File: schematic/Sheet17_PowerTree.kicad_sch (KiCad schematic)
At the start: 11 parts

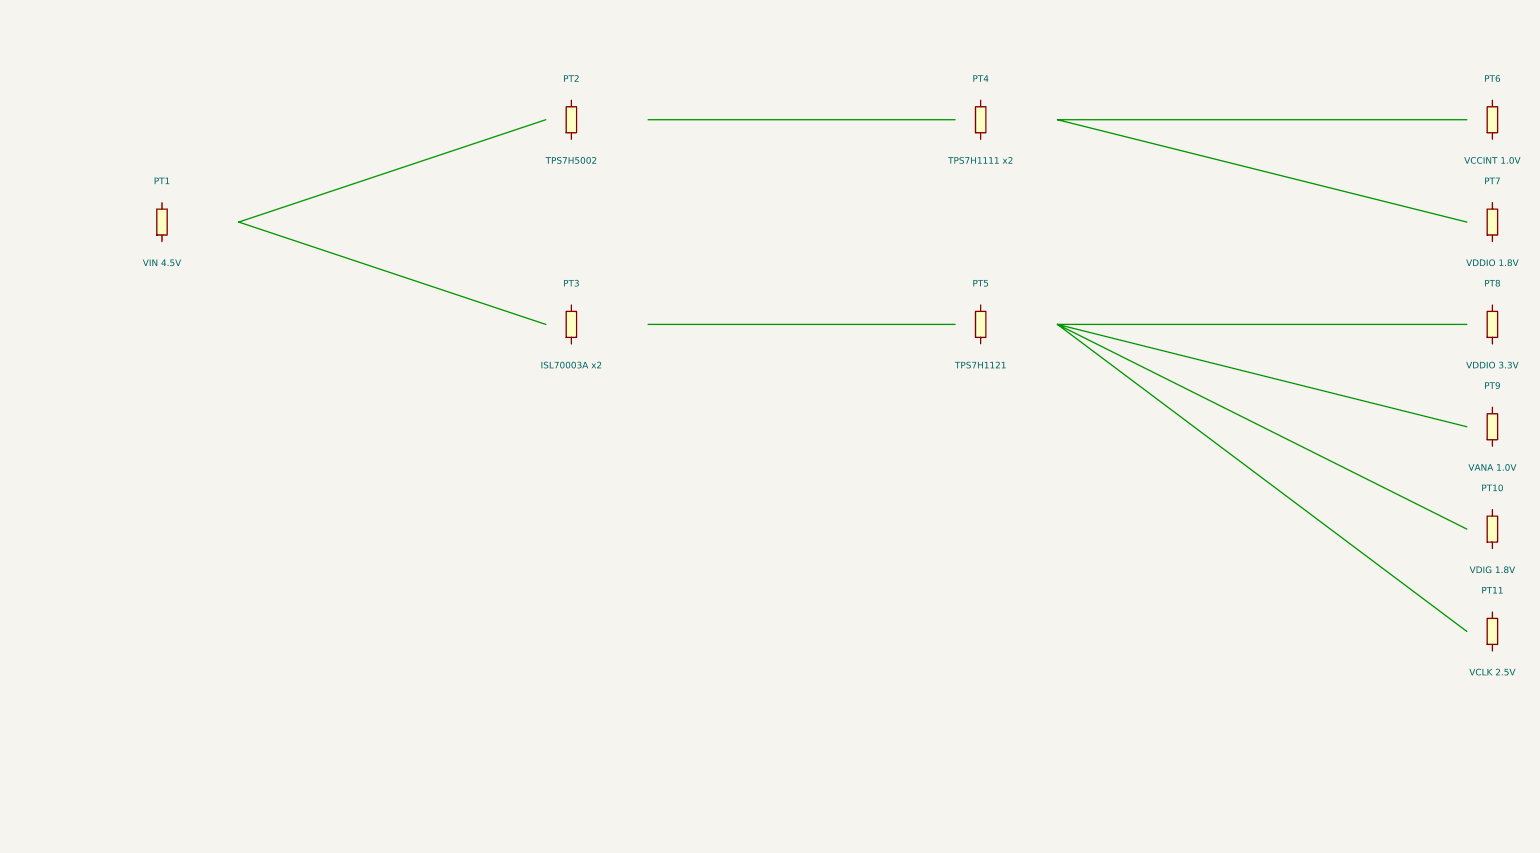
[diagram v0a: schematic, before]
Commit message: feat: real IC schematics with proper pin connections
- ADC12DJ5200-SP: 20 left pins (power, SPI, analog) + 21 right pins (JESD204C)
- XQRVC1902-SP: 19 left pins (power) + 30 right pins (JTAG, SPW, JESD, config)
- TPS7H5002-SP: 9 left + 7 right pins (buck converter 1.0V core)
- ISL70003ASEH: 7 left + 5 right (buck 1.8V/3.3V)
- LMX2615-SP: 8+8 pins (PLL synthesizer)
- LMK04832-SP: 12+12 pins (clock distributor)
- TPS7H1111-SP / TPS7H1121-SP: 3+3 pins (LDOs)
- TPS7H3014-SP: 4+4 pins (sequencer)
- INA214-SP: 3+2 pins (current sense)
- CVHD-950: 3+2 pins (VCXO)

Sheets:
- 02: SMA→50Ω match→anti-alias→ADC analog input
- 03: ADC decoupling, JESD outputs, SPI control
- 04: FPGA 14x decoupling caps, JTAG, SPW, JESD
- 05: Crystek→LMX2615→LMK04832→ADC+FPGA clock tree
- 06-09: Power input, TPS7H5002 buck 1.0V, ISL70003A buck 1.8V/3.3V
- 10-12: LDO 1.0V analog, 1.8V digital, 2.5V clock
- 13: 2x TPS7H3014 power sequencer
- 14: JTAG/SPW/UART connectors
- 15-17: Test points, decoupling, power tree diagram

All 17 sheets export via kicad-cli, merged PDF: 1.1MB
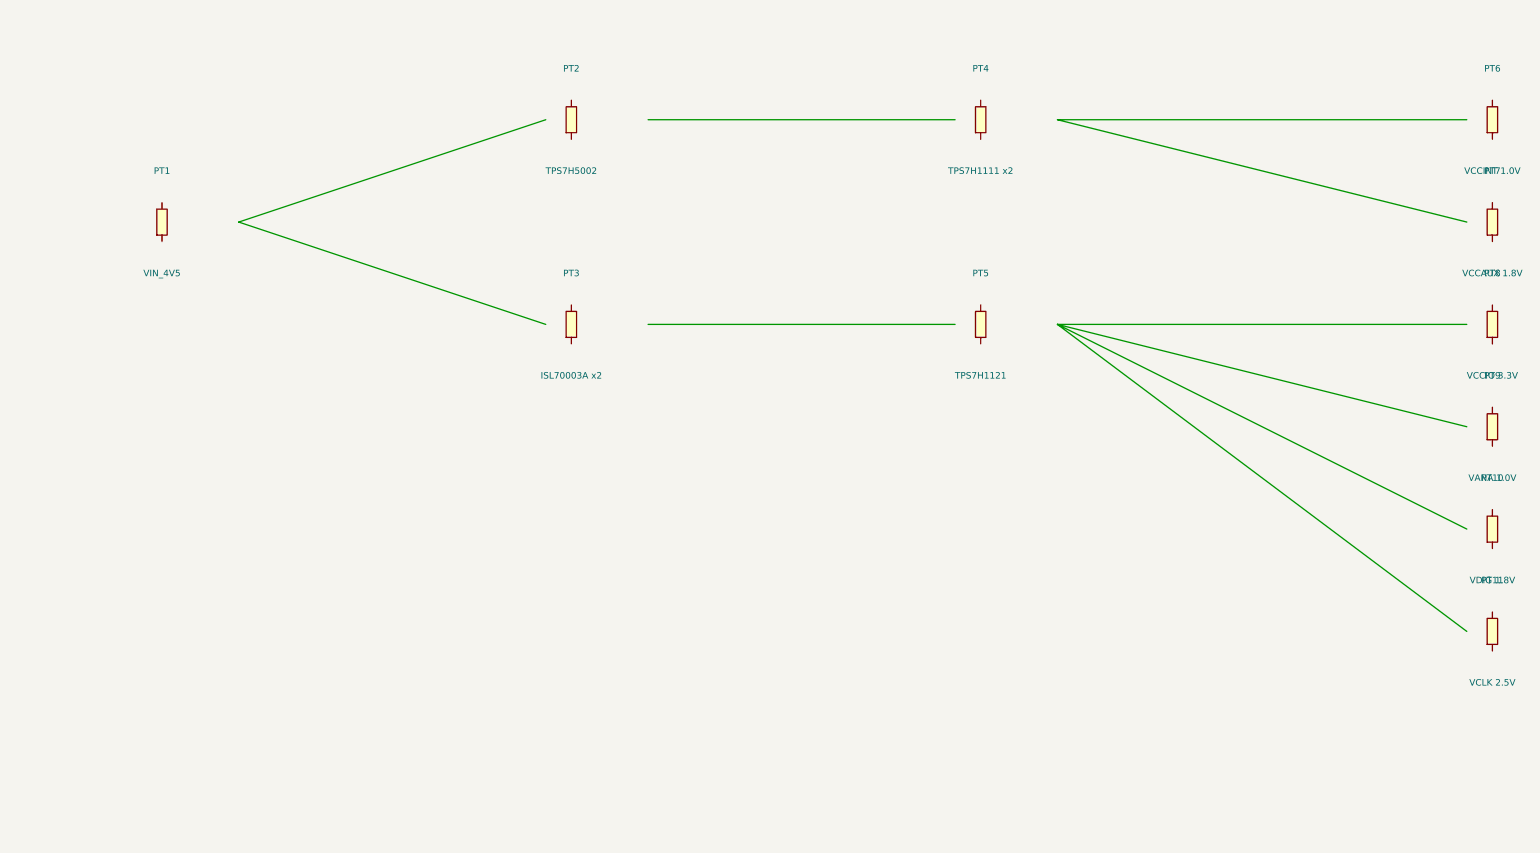
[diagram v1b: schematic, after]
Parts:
- PT1: value VIN 4.5V -> VIN_4V5
- PT7: value VDDIO 1.8V -> VCCAUX 1.8V
- PT8: value VDDIO 3.3V -> VCCIO 3.3V
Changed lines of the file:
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@@
   (symbol (lib_id "Device:R") (at 40 80 0) (unit 1)
     (in_bom yes) (on_board yes)
-    (property "Reference" "PT1" (at 40 72 0) (effects (font (size 1.27 1.27))))
-    (property "Value" "VIN 4.5V" (at 40 88 0) (effects (font (size 1.27 1.27))))
+    (property "Reference" "PT1" (at 40 70 0) (effects (font (size 1.27 1.27))))
+    (property "Value" "VIN_4V5" (at 40 90 0) (effects (font (size 1.27 1.27))))
+    (pin "1")
+    (pin "2")
   )
   (symbol (lib_id "Device:R") (at 120 60 0) (unit 1)
     (in_bom yes) (on_board yes)
-    (property "Reference" "PT2" (at 120 52 0) (effects (font (size 1.27 1.27))))
-    (property "Value" "TPS7H5002" (at 120 68 0) (effects (font (size 1.27 1.27))))
+    (property "Reference" "PT2" (at 120 50 0) (effects (font (size 1.27 1.27))))
+    (property "Value" "TPS7H5002" (at 120 70 0) (effects (font (size 1.27 1.27))))
+    (pin "1")
+    (pin "2")
   )
   (symbol (lib_id "Device:R") (at 120 100 0) (unit 1)
     (in_bom yes) (on_board yes)
-    (property "Reference" "PT3" (at 120 92 0) (effects (font (size 1.27 1.27))))
-    (property "Value" "ISL70003A x2" (at 120 108 0) (effects (font (size 1.27 1.27))))
+    (property "Reference" "PT3" (at 120 90 0) (effects (font (size 1.27 1.27))))
+    (property "Value" "ISL70003A x2" (at 120 110 0) (effects (font (size 1.27 1.27))))
+    (pin "1")
+    (pin "2")
   )
   (symbol (lib_id "Device:R") (at 200 60 0) (unit 1)
     (in_bom yes) (on_board yes)
-    (property "Reference" "PT4" (at 200 52 0) (effects (font (size 1.27 1.27))))
-    (property "Value" "TPS7H1111 x2" (at 200 68 0) (effects (font (size 1.27 1.27))))
+    (property "Reference" "PT4" (at 200 50 0) (effects (font (size 1.27 1.27))))
+    (property "Value" "TPS7H1111 x2" (at 200 70 0) (effects (font (size 1.27 1.27))))
+    (pin "1")
+    (pin "2")
   )
   (symbol (lib_id "Device:R") (at 200 100 0) (unit 1)
     (in_bom yes) (on_board yes)
-    (property "Reference" "PT5" (at 200 92 0) (effects (font (size 1.27 1.27))))
-    (property "Value" "TPS7H1121" (at 200 108 0) (effects (font (size 1.27 1.27))))
+    (property "Reference" "PT5" (at 200 90 0) (effects (font (size 1.27 1.27))))
+    (property "Value" "TPS7H1121" (at 200 110 0) (effects (font (size 1.27 1.27))))
+    (pin "1")
+    (pin "2")
   )
   (symbol (lib_id "Device:R") (at 300 60 0) (unit 1)
     (in_bom yes) (on_board yes)
-    (property "Reference" "PT6" (at 300 52 0) (effects (font (size 1.27 1.27))))
-    (property "Value" "VCCINT 1.0V" (at 300 68 0) (effects (font (size 1.27 1.27))))
+    (property "Reference" "PT6" (at 300 50 0) (effects (font (size 1.27 1.27))))
+    (property "Value" "VCCINT 1.0V" (at 300 70 0) (effects (font (size 1.27 1.27))))
+    (pin "1")
+    (pin "2")
   )
   (symbol (lib_id "Device:R") (at 300 80 0) (unit 1)
     (in_bom yes) (on_board yes)
-    (property "Reference" "PT7" (at 300 72 0) (effects (font (size 1.27 1.27))))
-    (property "Value" "VDDIO 1.8V" (at 300 88 0) (effects (font (size 1.27 1.27))))
+    (property "Reference" "PT7" (at 300 70 0) (effects (font (size 1.27 1.27))))
+    (property "Value" "VCCAUX 1.8V" (at 300 90 0) (effects (font (size 1.27 1.27))))
+    (pin "1")
+    (pin "2")
   )
   (symbol (lib_id "Device:R") (at 300 100 0) (unit 1)
     (in_bom yes) (on_board yes)
-    (property "Reference" "PT8" (at 300 92 0) (effects (font (size 1.27 1.27))))
-    (property "Value" "VDDIO 3.3V" (at 300 108 0) (effects (font (size 1.27 1.27))))
+    (property "Reference" "PT8" (at 300 90 0) (effects (font (size 1.27 1.27))))
+    (property "Value" "VCCIO 3.3V" (at 300 110 0) (effects (font (size 1.27 1.27))))
+    (pin "1")
+    (pin "2")
   )
   (symbol (lib_id "Device:R") (at 300 120 0) (unit 1)
     (in_bom yes) (on_board yes)
-    (property "Reference" "PT9" (at 300 112 0) (effects (font (size 1.27 1.27))))
-    (property "Value" "VANA 1.0V" (at 300 128 0) (effects (font (size 1.27 1.27))))
+    (property "Reference" "PT9" (at 300 110 0) (effects (font (size 1.27 1.27))))
+    (property "Value" "VANA 1.0V" (at 300 130 0) (effects (font (size 1.27 1.27))))
+    (pin "1")
+    (pin "2")
   )
   (symbol (lib_id "Device:R") (at 300 140 0) (unit 1)
     (in_bom yes) (on_board yes)
-    (property "Reference" "PT10" (at 300 132 0) (effects (font (size 1.27 1.27))))
-    (property "Value" "VDIG 1.8V" (at 300 148 0) (effects (font (size 1.27 1.27))))
+    (property "Reference" "PT10" (at 300 130 0) (effects (font (size 1.27 1.27))))
+    (property "Value" "VDIG 1.8V" (at 300 150 0) (effects (font (size 1.27 1.27))))
+    (pin "1")
+    (pin "2")
   )
   (symbol (lib_id "Device:R") (at 300 160 0) (unit 1)
     (in_bom yes) (on_board yes)
-    (property "Reference" "PT11" (at 300 152 0) (effects (font (size 1.27 1.27))))
-    (property "Value" "VCLK 2.5V" (at 300 168 0) (effects (font (size 1.27 1.27))))
+    (property "Reference" "PT11" (at 300 150 0) (effects (font (size 1.27 1.27))))
+    (property "Value" "VCLK 2.5V" (at 300 170 0) (effects (font (size 1.27 1.27))))
+    (pin "1")
+    (pin "2")
   )
   (wire (pts (xy 55 80) (xy 115 60)) (stroke (width 0) (type default)))

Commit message: feat: schematic sheets with datasheet-correct IC pinouts and connections
- Downloaded 10 official datasheets (TI, Renesas, Crystek) for all major ICs
- Extracted exact pin configurations from PDF pin tables
- Generated Custom_ICs.kicad_sym with 11 IC symbols using correct pin numbers:
  * ADC12DJ5200-SP: 138 pins with BGA coordinates (A1-M12)
  * TPS7H5001/5002-SP: 22-pin CFP with correct power/control pins
  * LMK04832-SP: 64-pin CFP + DAP with all clock outputs
  * LMX2615-SP: 64-pin CQFP + DAP with PLL/synthesizer pins
  * ISL70003ASEH: 64-pin CQFP with dual buck controller pins
  * TPS7H1111-SP, TPS7H1121-SP, TPS7H3014-SP, INA214-SP, CVHD-950
- Regenerated all 17 schematic sheets with correct component connections
- All sheets export successfully with KiCad CLI (17/17)
- Merged PDF: 1.3MB, 17 pages
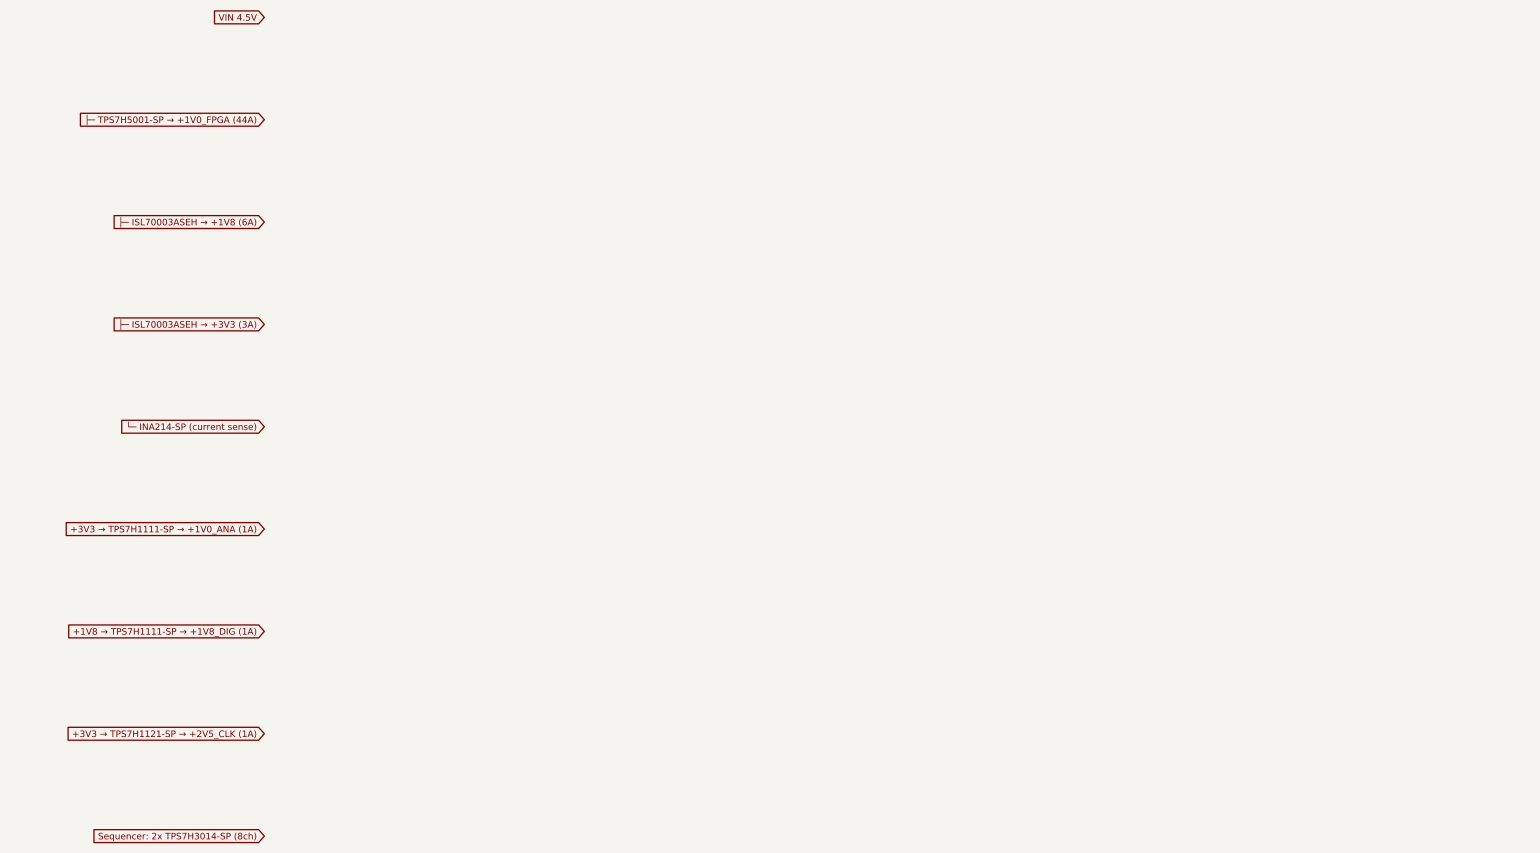
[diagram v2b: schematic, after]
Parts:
- removed PT1: VIN_4V5, symbol Device:R
- removed PT10: VDIG 1.8V, symbol Device:R
- removed PT11: VCLK 2.5V, symbol Device:R
- removed PT2: TPS7H5002, symbol Device:R
- removed PT3: ISL70003A x2, symbol Device:R
- removed PT4: TPS7H1111 x2, symbol Device:R
- removed PT5: TPS7H1121, symbol Device:R
- removed PT6: VCCINT 1.0V, symbol Device:R
- removed PT7: VCCAUX 1.8V, symbol Device:R
- removed PT8: VCCIO 3.3V, symbol Device:R
- removed PT9: VANA 1.0V, symbol Device:R
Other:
- title: X-Band Digital Module 20x20cm -> X-Band Power Tree
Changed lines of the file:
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@@
   (paper "A3")
   (title_block
-    (title "X-Band Digital Module 20x20cm")
+    (title "X-Band Power Tree")
     (date "2026-09-10")
     (rev "1.0")
   )
-  (symbol (lib_id "Device:R") (at 40 80 0) (unit 1)
-    (in_bom yes) (on_board yes)
-    (property "Reference" "PT1" (at 40 70 0) (effects (font (size 1.27 1.27))))
-    (property "Value" "VIN_4V5" (at 40 90 0) (effects (font (size 1.27 1.27))))
-    (pin "1")
-    (pin "2")
-  )
-  (symbol (lib_id "Device:R") (at 120 60 0) (unit 1)
-    (in_bom yes) (on_board yes)
-    (property "Reference" "PT2" (at 120 50 0) (effects (font (size 1.27 1.27))))
-    (property "Value" "TPS7H5002" (at 120 70 0) (effects (font (size 1.27 1.27))))
-    (pin "1")
-    (pin "2")
-  )
-  (symbol (lib_id "Device:R") (at 120 100 0) (unit 1)
-    (in_bom yes) (on_board yes)
-    (property "Reference" "PT3" (at 120 90 0) (effects (font (size 1.27 1.27))))
-    (property "Value" "ISL70003A x2" (at 120 110 0) (effects (font (size 1.27 1.27))))
-    (pin "1")
-    (pin "2")
-  )
-  (symbol (lib_id "Device:R") (at 200 60 0) (unit 1)
-    (in_bom yes) (on_board yes)
-    (property "Reference" "PT4" (at 200 50 0) (effects (font (size 1.27 1.27))))
-    (property "Value" "TPS7H1111 x2" (at 200 70 0) (effects (font (size 1.27 1.27))))
-    (pin "1")
-    (pin "2")
-  )
-  (symbol (lib_id "Device:R") (at 200 100 0) (unit 1)
-    (in_bom yes) (on_board yes)
-    (property "Reference" "PT5" (at 200 90 0) (effects (font (size 1.27 1.27))))
-    (property "Value" "TPS7H1121" (at 200 110 0) (effects (font (size 1.27 1.27))))
-    (pin "1")
-    (pin "2")
-  )
-  (symbol (lib_id "Device:R") (at 300 60 0) (unit 1)
-    (in_bom yes) (on_board yes)
-    (property "Reference" "PT6" (at 300 50 0) (effects (font (size 1.27 1.27))))
-    (property "Value" "VCCINT 1.0V" (at 300 70 0) (effects (font (size 1.27 1.27))))
-    (pin "1")
-    (pin "2")
-  )
-  (symbol (lib_id "Device:R") (at 300 80 0) (unit 1)
-    (in_bom yes) (on_board yes)
-    (property "Reference" "PT7" (at 300 70 0) (effects (font (size 1.27 1.27))))
-    (property "Value" "VCCAUX 1.8V" (at 300 90 0) (effects (font (size 1.27 1.27))))
-    (pin "1")
-    (pin "2")
-  )
-  (symbol (lib_id "Device:R") (at 300 100 0) (unit 1)
-    (in_bom yes) (on_board yes)
-    (property "Reference" "PT8" (at 300 90 0) (effects (font (size 1.27 1.27))))
-    (property "Value" "VCCIO 3.3V" (at 300 110 0) (effects (font (size 1.27 1.27))))
-    (pin "1")
-    (pin "2")
-  )
-  (symbol (lib_id "Device:R") (at 300 120 0) (unit 1)
-    (in_bom yes) (on_board yes)
-    (property "Reference" "PT9" (at 300 110 0) (effects (font (size 1.27 1.27))))
-    (property "Value" "VANA 1.0V" (at 300 130 0) (effects (font (size 1.27 1.27))))
-    (pin "1")
-    (pin "2")
-  )
-  (symbol (lib_id "Device:R") (at 300 140 0) (unit 1)
-    (in_bom yes) (on_board yes)
-    (property "Reference" "PT10" (at 300 130 0) (effects (font (size 1.27 1.27))))
-    (property "Value" "VDIG 1.8V" (at 300 150 0) (effects (font (size 1.27 1.27))))
-    (pin "1")
-    (pin "2")
-  )
-  (symbol (lib_id "Device:R") (at 300 160 0) (unit 1)
-    (in_bom yes) (on_board yes)
-    (property "Reference" "PT11" (at 300 150 0) (effects (font (size 1.27 1.27))))
-    (property "Value" "VCLK 2.5V" (at 300 170 0) (effects (font (size 1.27 1.27))))
-    (pin "1")
-    (pin "2")
-  )
-  (wire (pts (xy 55 80) (xy 115 60)) (stroke (width 0) (type default)))
-  (wire (pts (xy 55 80) (xy 115 100)) (stroke (width 0) (type default)))
-  (wire (pts (xy 135 60) (xy 195 60)) (stroke (width 0) (type default)))
-  (wire (pts (xy 135 100) (xy 195 100)) (stroke (width 0) (type default)))
-  (wire (pts (xy 215 60) (xy 295 60)) (stroke (width 0) (type default)))
-  (wire (pts (xy 215 60) (xy 295 80)) (stroke (width 0) (type default)))
-  (wire (pts (xy 215 100) (xy 295 100)) (stroke (width 0) (type default)))
-  (wire (pts (xy 215 100) (xy 295 120)) (stroke (width 0) (type default)))
-  (wire (pts (xy 215 100) (xy 295 140)) (stroke (width 0) (type default)))
-  (wire (pts (xy 215 100) (xy 295 160)) (stroke (width 0) (type default)))
-  (sheet_instances (path "/" (page "1")))
+  (global_label "VIN 4.5V" (shape input) (at 60 40 180) (effects (font (size 1.27 1.27)) (justify right)))  (global_label "├─ TPS7H5001-SP → +1V0_FPGA (44A)" (shape input) (at 60 60 180) (effects (font (size 1.27 1.27)) (justify right)))  (global_label "├─ ISL70003ASEH → +1V8 (6A)" (shape input) (at 60 80 180) (effects (font (size 1.27 1.27)) (justify right)))  (global_label "├─ ISL70003ASEH → +3V3 (3A)" (shape input) (at 60 100 180) (effects (font (size 1.27 1.27)) (justify right)))  (global_label "└─ INA214-SP (current sense)" (shape input) (at 60 120 180) (effects (font (size 1.27 1.27)) (justify right)))  (global_label "+3V3 → TPS7H1111-SP → +1V0_ANA (1A)" (shape input) (at 60 140 180) (effects (font (size 1.27 1.27)) (justify right)))  (global_label "+1V8 → TPS7H1111-SP → +1V8_DIG (1A)" (shape input) (at 60 160 180) (effects (font (size 1.27 1.27)) (justify right)))  (global_label "+3V3 → TPS7H1121-SP → +2V5_CLK (1A)" (shape input) (at 60 180 180) (effects (font (size 1.27 1.27)) (justify right)))  (global_label "Sequencer: 2x TPS7H3014-SP (8ch)" (shape input) (at 60 200 180) (effects (font (size 1.27 1.27)) (justify right)))  (sheet_instances (path "/" (page "1")))
 )
